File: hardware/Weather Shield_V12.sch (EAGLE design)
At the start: 48 parts, among them J1 GP-635T, Q1 BSS138, Q2 BSS138, U1 ARDUINO_R3_SHIELD, U2 3.3V MIC5219, U3 ALS-PT19, U4 MPL3115A2LGA8, U5 HTU21D

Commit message: V1.2 Initial Checklist pushes
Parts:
- removed U5: HTU21D, SparkFun-Sensors:HTU21DSMD
- added FD1, FD2: FIDUCIAL1X2, SparkFun-Aesthetics:FIDUCIAL1X2
- added U$1: SI7021, SparkFun-Sensors:SI7021
- added U$2: REVISION, SparkFun-Aesthetics:REVISION
- S2: value Serial Select -> DPDT
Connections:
- net 3.3V: now also U$1.VDD; no longer U5.VDD
- net GND: now also U$1.GND; no longer U5.GND@2, U5.GND@7
- net SCL: now also U$1.SCK; no longer U5.SCK
- net SDA: now also U$1.DATA; no longer U5.DATA
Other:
- note added: "Customer/Comment complaints and suggested changes"
- note added: "Input Voltage Range: 5-12V"
- note added: "Joel Bartlett"
- note added: "Rain gauges share same pins as XBee shield"
- note added: "V1.2"
- note removed: "Added 3.3V hook to A3 for 5>VCC>3.3V operation"
- note removed: "Changes on v1.1:"
- note removed: "Corrected GP-635T footprint"
- note removed: "Removed 3.6V Zener"
- note removed: "Removed TEMT6000 light sensor"
- note removed: "V1.1"

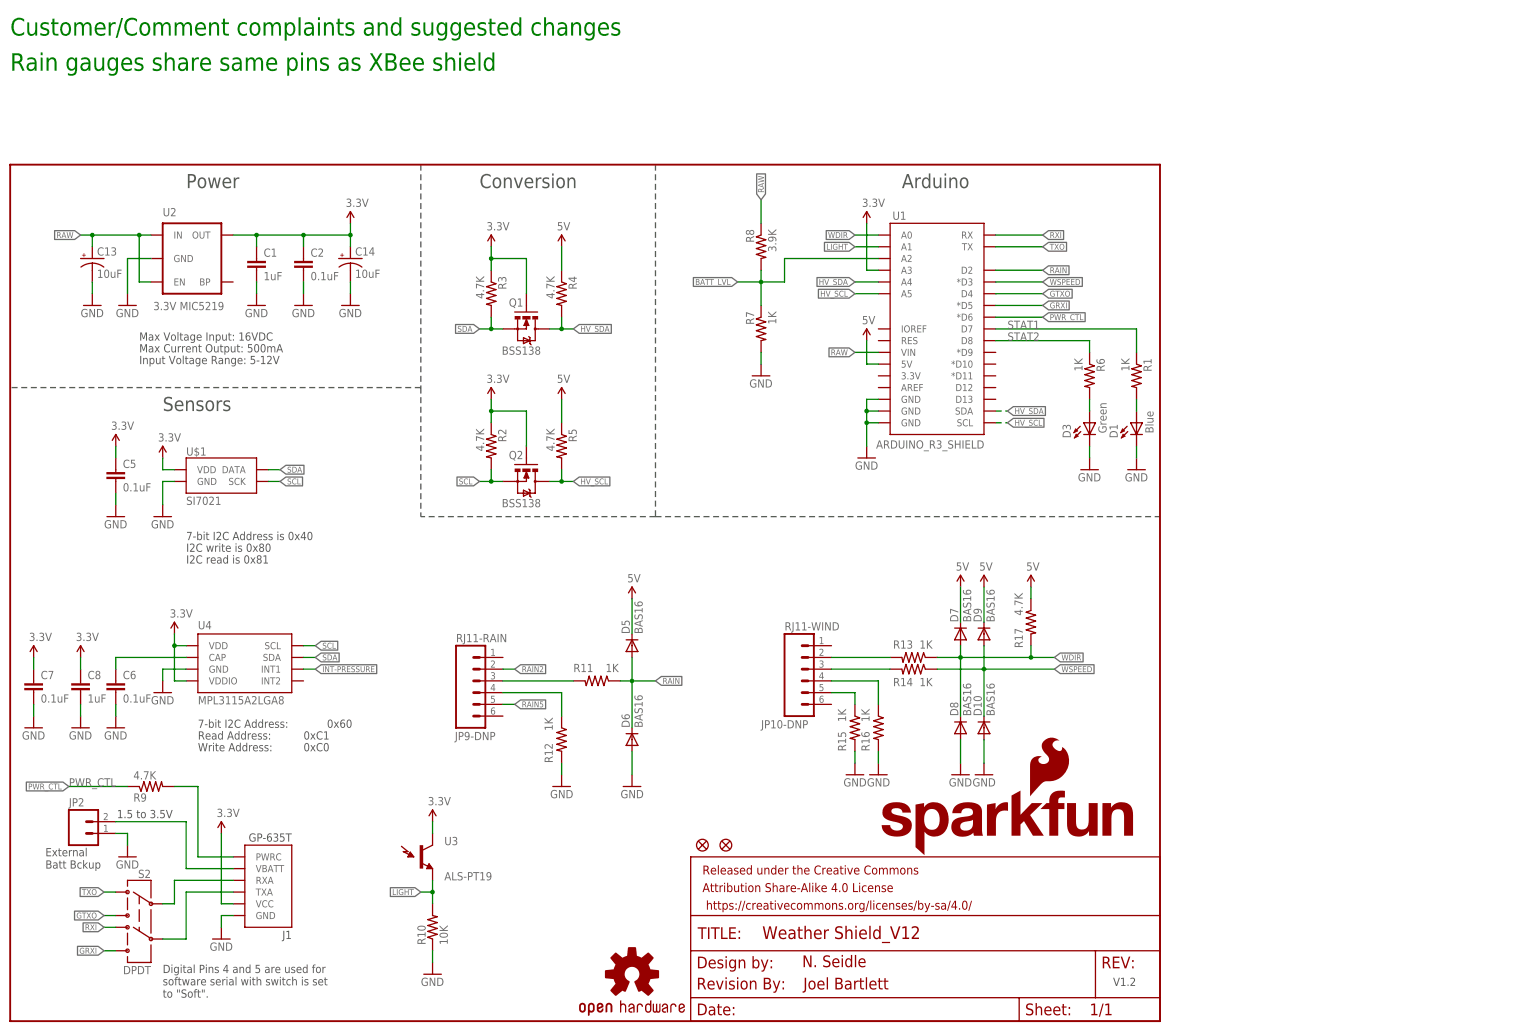
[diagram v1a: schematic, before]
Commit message: Fixed 4-way junctions
Fixed 4-way junctions
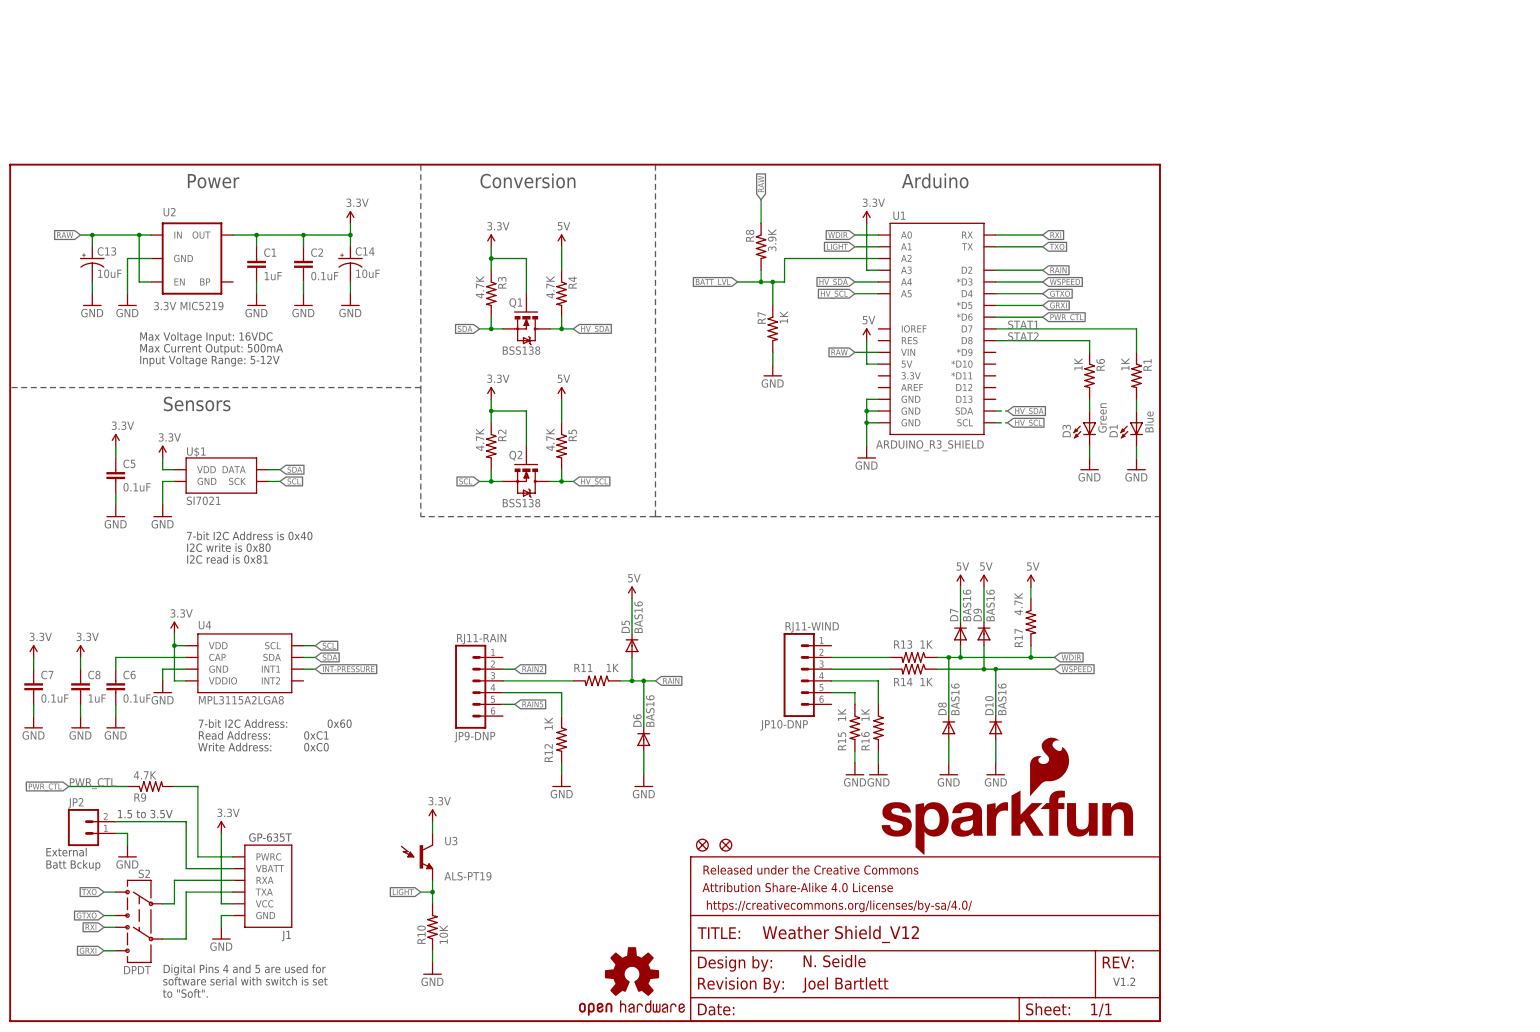
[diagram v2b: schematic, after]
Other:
- note removed: "Customer/Comment complaints and suggested changes"
- note removed: "Rain gauges share same pins as XBee shield"
- moved on the sheet: D10, D6, D8, R7
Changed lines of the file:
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@@
 software serial with switch is set
 to "Soft".</text>
-<text x="0" y="213.36" size="3.81" layer="91">Customer/Comment complaints and suggested changes</text>
-<text x="0" y="205.74" size="3.81" layer="91">Rain gauges share same pins as XBee shield</text>
 <text x="171.704" y="6.858" size="2.54" layer="94">Joel Bartlett</text>
 <text x="27.94" y="142.24" size="1.778" layer="97">Input Voltage Range: 5-12V</text>
@@
 </instance>
 <instance part="D9" gate="G$1" x="210.82" y="83.82" rot="R90"/>
-<instance part="D10" gate="G$1" x="210.82" y="63.5" rot="R90"/>
+<instance part="D10" gate="G$1" x="213.36" y="63.5" rot="R90"/>
 <instance part="D7" gate="G$1" x="205.74" y="83.82" rot="R90"/>
-<instance part="D8" gate="G$1" x="205.74" y="63.5" rot="R90"/>
+<instance part="D8" gate="G$1" x="203.2" y="63.5" rot="R90"/>
 <instance part="D5" gate="G$1" x="134.62" y="81.28" rot="R90"/>
-<instance part="D6" gate="G$1" x="134.62" y="60.96" rot="R90"/>
-<instance part="GND21" gate="1" x="210.82" y="53.34" rot="MR0"/>
-<instance part="GND29" gate="1" x="205.74" y="53.34"/>
-<instance part="GND31" gate="1" x="134.62" y="50.8" rot="MR0"/>
+<instance part="D6" gate="G$1" x="137.16" y="60.96" rot="R90"/>
+<instance part="GND21" gate="1" x="213.36" y="53.34" rot="MR0"/>
+<instance part="GND29" gate="1" x="203.2" y="53.34"/>
+<instance part="GND31" gate="1" x="137.16" y="50.8" rot="MR0"/>
 <instance part="R12" gate="G$1" x="119.38" y="60.96" smashed="yes" rot="R270">
 <attribute name="NAME" x="117.475" y="55.88" size="1.778" layer="95" rot="R90"/>
@@
 <instance part="SUPPLY10" gate="G$1" x="134.62" y="91.44"/>
 <instance part="LOGO2" gate="G$1" x="187.96" y="35.56"/>
-<instance part="R7" gate="G$1" x="162.56" y="149.86" rot="MR270"/>
+<instance part="R7" gate="G$1" x="165.1" y="149.86" rot="MR270"/>
 <instance part="R8" gate="G$1" x="162.56" y="167.64" rot="MR270"/>
-<instance part="GND28" gate="1" x="162.56" y="139.7"/>
+<instance part="GND28" gate="1" x="165.1" y="139.7"/>
 <instance part="LOGO1" gate="G$1" x="134.62" y="10.16"/>
 <instance part="R9" gate="G$1" x="30.48" y="50.8" rot="MR180"/>
@@
 </segment>
 <segment>
-<wire x1="210.82" y1="55.88" x2="210.82" y2="60.96" width="0.1524" layer="91"/>
+<wire x1="213.36" y1="55.88" x2="213.36" y2="60.96" width="0.1524" layer="91"/>
 <pinref part="GND21" gate="1" pin="GND"/>
 <pinref part="D10" gate="G$1" pin="A"/>
 </segment>
 <segment>
-<wire x1="205.74" y1="55.88" x2="205.74" y2="60.96" width="0.1524" layer="91"/>
+<wire x1="203.2" y1="55.88" x2="203.2" y2="60.96" width="0.1524" layer="91"/>
 <pinref part="GND29" gate="1" pin="GND"/>
 <pinref part="D8" gate="G$1" pin="A"/>
 </segment>
 <segment>
-<wire x1="134.62" y1="53.34" x2="134.62" y2="58.42" width="0.1524" layer="91"/>
+<wire x1="137.16" y1="53.34" x2="137.16" y2="58.42" width="0.1524" layer="91"/>
 <pinref part="GND31" gate="1" pin="GND"/>
 <pinref part="D6" gate="G$1" pin="A"/>
@@
 </segment>
 <segment>
-<wire x1="162.56" y1="142.24" x2="162.56" y2="144.78" width="0.1524" layer="91"/>
+<wire x1="165.1" y1="142.24" x2="165.1" y2="144.78" width="0.1524" layer="91"/>
 <pinref part="R7" gate="G$1" pin="2"/>
 <pinref part="GND28" gate="1" pin="GND"/>
@@
 <segment>
 <wire x1="132.08" y1="73.66" x2="134.62" y2="73.66" width="0.1524" layer="91"/>
-<wire x1="134.62" y1="73.66" x2="139.7" y2="73.66" width="0.1524" layer="91"/>
-<wire x1="134.62" y1="63.5" x2="134.62" y2="73.66" width="0.1524" layer="91"/>
+<wire x1="134.62" y1="73.66" x2="137.16" y2="73.66" width="0.1524" layer="91"/>
+<wire x1="137.16" y1="73.66" x2="139.7" y2="73.66" width="0.1524" layer="91"/>
 <wire x1="134.62" y1="73.66" x2="134.62" y2="78.74" width="0.1524" layer="91"/>
 <junction x="134.62" y="73.66"/>
 <pinref part="R11" gate="G$1" pin="1"/>
-<pinref part="D6" gate="G$1" pin="C"/>
 <pinref part="D5" gate="G$1" pin="A"/>
 <label x="139.7" y="73.66" size="1.27" layer="95" xref="yes"/>
+<pinref part="D6" gate="G$1" pin="C"/>
+<wire x1="137.16" y1="63.5" x2="137.16" y2="73.66" width="0.1524" layer="91"/>
+<junction x="137.16" y="73.66"/>
 </segment>
 <segment>
@@
 <segment>
 <wire x1="200.66" y1="76.2" x2="210.82" y2="76.2" width="0.1524" layer="91"/>
-<wire x1="210.82" y1="76.2" x2="226.06" y2="76.2" width="0.1524" layer="91"/>
+<wire x1="210.82" y1="76.2" x2="213.36" y2="76.2" width="0.1524" layer="91"/>
+<wire x1="213.36" y1="76.2" x2="226.06" y2="76.2" width="0.1524" layer="91"/>
 <wire x1="210.82" y1="81.28" x2="210.82" y2="76.2" width="0.1524" layer="91"/>
-<wire x1="210.82" y1="76.2" x2="210.82" y2="66.04" width="0.1524" layer="91"/>
 <junction x="210.82" y="76.2"/>
 <pinref part="R14" gate="G$1" pin="1"/>
 <pinref part="D9" gate="G$1" pin="A"/>
+<label x="226.06" y="76.2" size="1.27" layer="95" xref="yes"/>
 <pinref part="D10" gate="G$1" pin="C"/>
-<label x="226.06" y="76.2" size="1.27" layer="95" xref="yes"/>
+<wire x1="213.36" y1="66.04" x2="213.36" y2="76.2" width="0.1524" layer="91"/>
+<junction x="213.36" y="76.2"/>
 </segment>
 <segment>
@@
 <net name="WDIR" class="0">
 <segment>
-<wire x1="200.66" y1="78.74" x2="205.74" y2="78.74" width="0.1524" layer="91"/>
+<wire x1="200.66" y1="78.74" x2="203.2" y2="78.74" width="0.1524" layer="91"/>
+<wire x1="203.2" y1="78.74" x2="205.74" y2="78.74" width="0.1524" layer="91"/>
 <wire x1="205.74" y1="78.74" x2="220.98" y2="78.74" width="0.1524" layer="91"/>
 <wire x1="220.98" y1="78.74" x2="226.06" y2="78.74" width="0.1524" layer="91"/>
 <wire x1="220.98" y1="81.28" x2="220.98" y2="78.74" width="0.1524" layer="91"/>
-<wire x1="205.74" y1="66.04" x2="205.74" y2="78.74" width="0.1524" layer="91"/>
 <wire x1="205.74" y1="81.28" x2="205.74" y2="78.74" width="0.1524" layer="91"/>
 <junction x="220.98" y="78.74"/>
@@
 <pinref part="R17" gate="G$1" pin="2"/>
 <pinref part="R13" gate="G$1" pin="1"/>
-<pinref part="D8" gate="G$1" pin="C"/>
 <pinref part="D7" gate="G$1" pin="A"/>
 <label x="226.06" y="78.74" size="1.27" layer="95" xref="yes"/>
+<pinref part="D8" gate="G$1" pin="C"/>
+<wire x1="203.2" y1="66.04" x2="203.2" y2="78.74" width="0.1524" layer="91"/>
+<junction x="203.2" y="78.74"/>
 </segment>
 <segment>
@@
 <wire x1="157.48" y1="160.02" x2="162.56" y2="160.02" width="0.1524" layer="91"/>
 <wire x1="162.56" y1="160.02" x2="162.56" y2="162.56" width="0.1524" layer="91"/>
-<wire x1="162.56" y1="160.02" x2="162.56" y2="154.94" width="0.1524" layer="91"/>
 <junction x="162.56" y="160.02"/>
 <pinref part="R8" gate="G$1" pin="2"/>
-<pinref part="R7" gate="G$1" pin="1"/>
 <label x="157.48" y="160.02" size="1.27" layer="95" rot="R180" xref="yes"/>
 <pinref part="U1" gate="G$1" pin="A2"/>
 <wire x1="187.96" y1="165.1" x2="167.64" y2="165.1" width="0.1524" layer="91"/>
 <wire x1="167.64" y1="165.1" x2="167.64" y2="160.02" width="0.1524" layer="91"/>
-<wire x1="167.64" y1="160.02" x2="162.56" y2="160.02" width="0.1524" layer="91"/>
-</segment>
-</net>
+<wire x1="167.64" y1="160.02" x2="165.1" y2="160.02" width="0.1524" layer="91"/>
+<pinref part="R7" gate="G$1" pin="1"/>
+<wire x1="165.1" y1="160.02" x2="162.56" y2="160.02" width="0.1524" layer="91"/>
+<wire x1="165.1" y1="154.94" x2="165.1" y2="160.02" width="0.1524" layer="91"/>
+<junction x="165.1" y="160.02"/>
+</segment>
+</net>
